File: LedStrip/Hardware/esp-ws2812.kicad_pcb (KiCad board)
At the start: 2 copper layers, 11 parts, among them P3 CONN_01X01, P4 CONN_01X02, Q1 BSS138, U1 MCP1700, U2 ESP-01v090

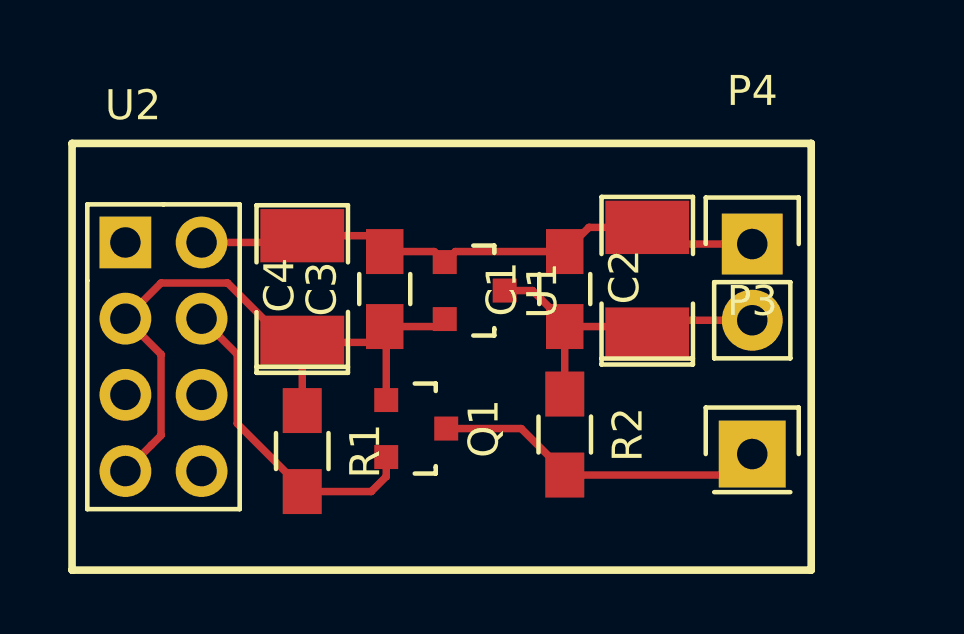
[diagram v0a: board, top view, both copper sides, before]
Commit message: finished up the layout of the board
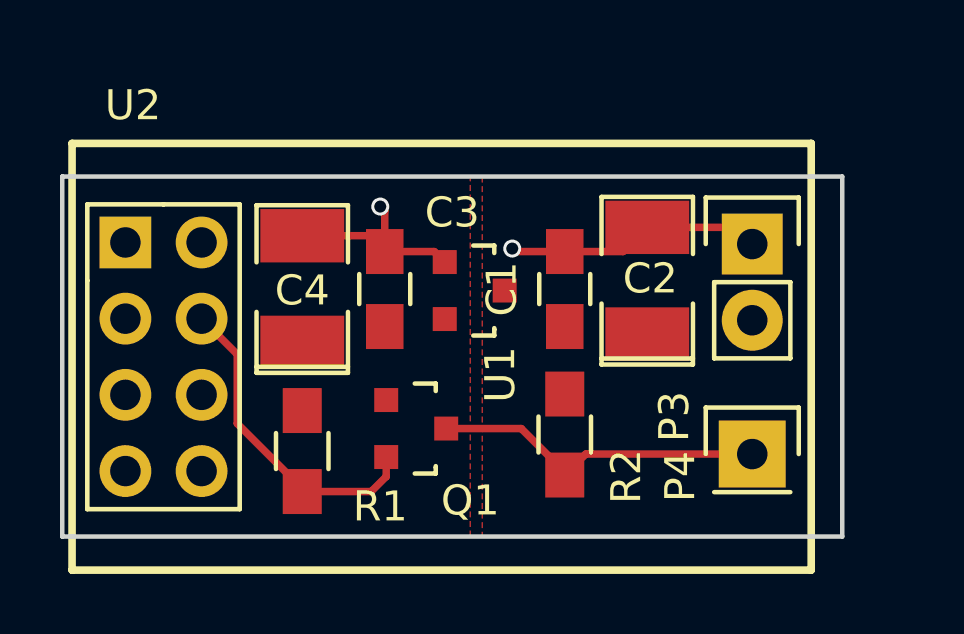
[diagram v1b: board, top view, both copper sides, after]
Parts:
- C1, C3: value C -> 0.1uf
- C2, C4: value CP -> 2.2uf
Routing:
- net +3V3: track 23.1 -> 0.00 mm
- net +5V: track 11.4 -> 0.00 mm
- net GND: track 19.5 -> 15.3 mm, vias 0 -> 2
- added copper zone on F.Cu, net +3V3
- added copper zone on F.Cu, net +5V
- added copper zone on B.Cu, net GND
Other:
- board outline added: 26 x 12 mm
- board text added: "Takigama - HAStrip me@pjr.cc DO NOT POWER LIGHTS FROM BOARD"

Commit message: new circuit board with power passthru
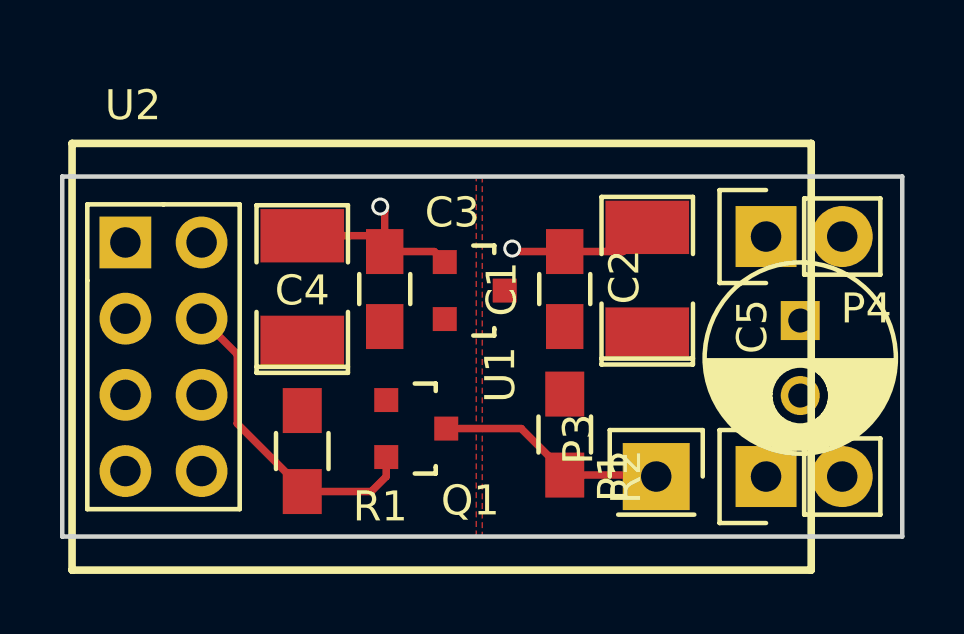
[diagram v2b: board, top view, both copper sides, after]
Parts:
- added C5: 1000uf, Capacitors_ThroughHole:C_Radial_D6.3_L11.2_P2.5, F.Cu at (174.6, 94.8)
- added P1: CONN_01X02, Pin_Headers:Pin_Header_Straight_1x02, F.Cu at (173.5, 100.0)
- moved P3 3.29 mm to (169.8, 100.0)
- moved P4 0.52 mm to (173.5, 92.0), turned to 90 degrees
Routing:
- net GND: track 15.3 -> 11.6 mm
- net GPIO2_5: track 11.2 -> 7.72 mm
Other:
- board size 26 x 12 mm -> 28 x 12 mm
- board text added: "Takigama - HAStrip me@pjr.cc"
- board text removed: "Takigama - HAStrip me@pjr.cc DO NOT POWER LIGHTS FROM BOARD"
